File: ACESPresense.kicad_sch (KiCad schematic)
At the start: 16 parts, among them U1 ESP32-WROOM-32D

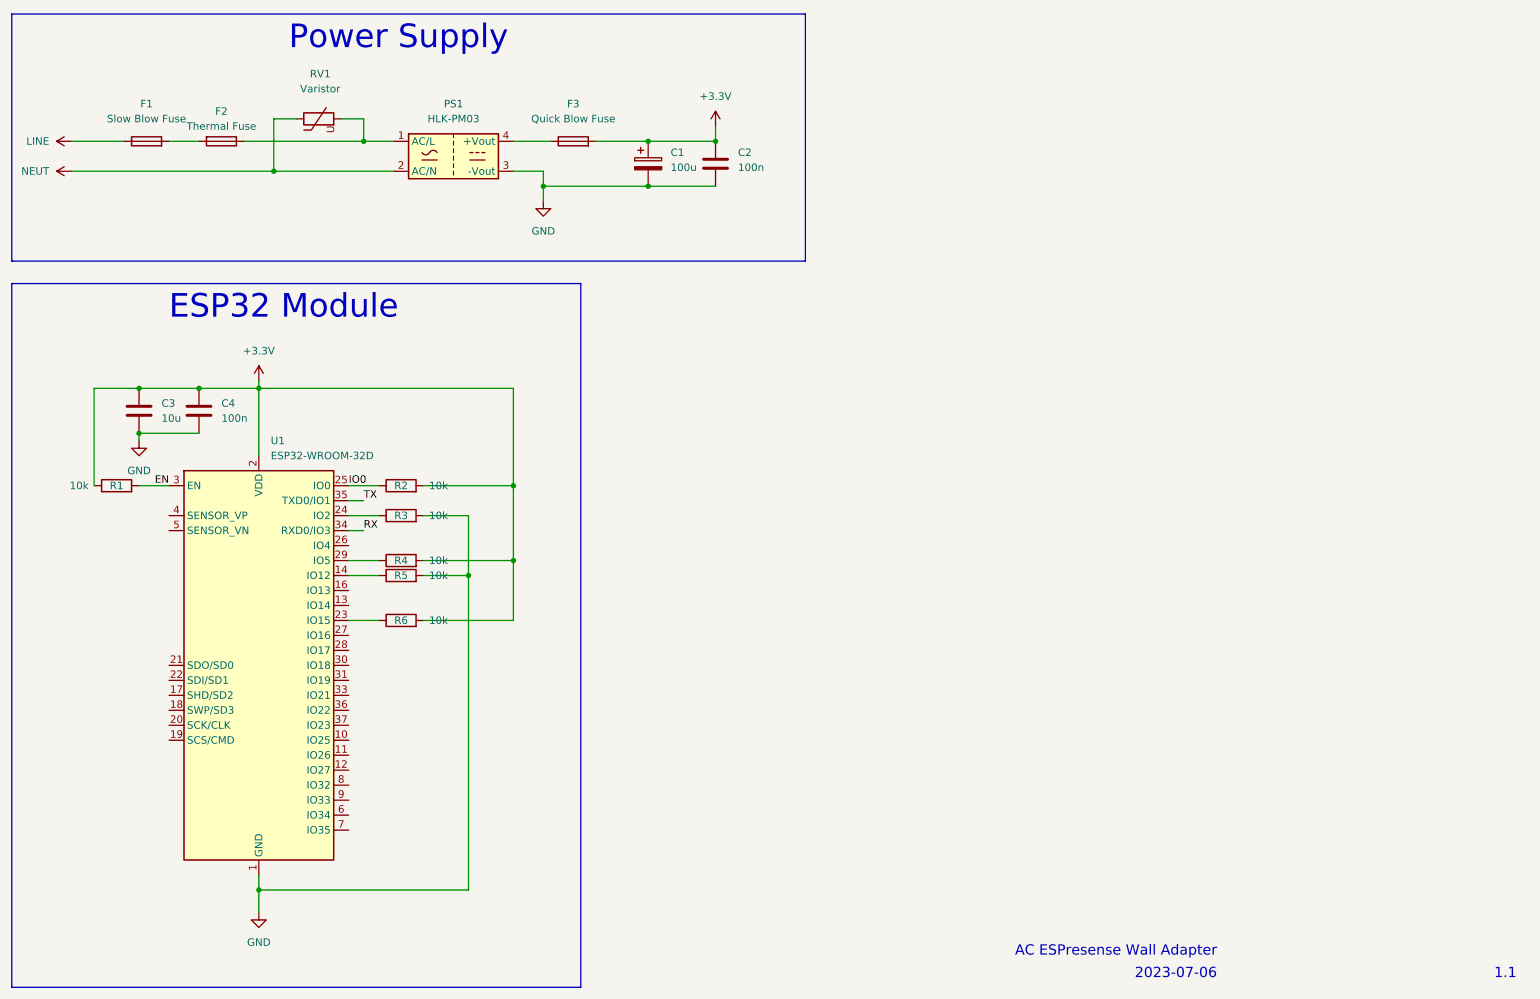
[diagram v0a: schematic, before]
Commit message: Added test points and fixed file names internally
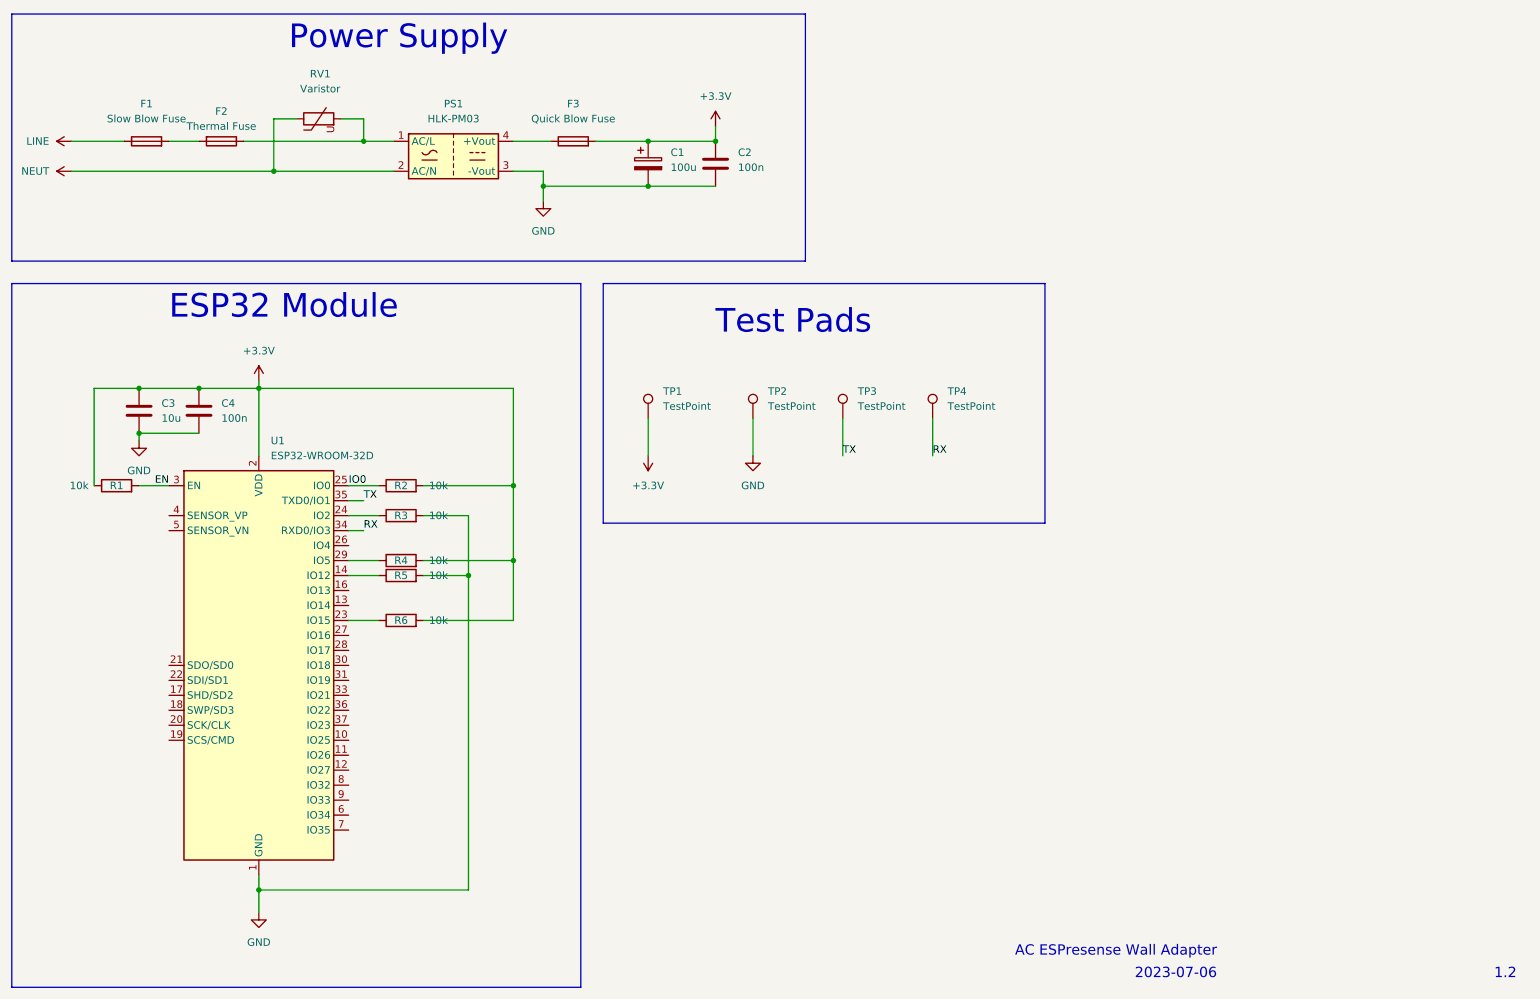
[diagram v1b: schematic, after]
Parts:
- added TP1, TP2, TP3, TP4: TestPoint, TestPoint:TestPoint_Pad_D2.0mm, symbol Connector:TestPoint
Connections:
- net +3.3V: now also TP1.1
- net GND: now also TP2.1
- net RX: now also TP4.1
- net TX: now also TP3.1
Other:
- note added: "1.2"
- note added: "Test Pads"
- note removed: "1.1"
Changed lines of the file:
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@@
+    (stroke (width 0) (type default))
+  )
+  (wire (pts (xy 124.46 99.06) (xy 124.46 105.41))
     (stroke (width 0) (type default))
   )
@@
     (stroke (width 0) (type default))
   )
+  (wire (pts (xy 142.24 99.06) (xy 142.24 105.41))
+    (stroke (width 0) (type default))
+  )
   (wire (pts (xy 106.68 59.69) (xy 124.46 59.69))
     (stroke (width 0) (type default))
@@
     (stroke (width 0) (type default))
   )
+  (wire (pts (xy 172.72 99.06) (xy 172.72 105.41))
+    (stroke (width 0) (type default))
+  )
   (wire (pts (xy 73.66 113.03) (xy 76.2 113.03))
     (stroke (width 0) (type default))
@@
     (stroke (width 0) (type default))
   )
+  (wire (pts (xy 157.48 99.06) (xy 157.48 105.41))
+    (stroke (width 0) (type default))
+  )
   (wire (pts (xy 135.89 49.53) (xy 135.89 52.07))
     (stroke (width 0) (type default))
@@
     (stroke (width 0) (type default))
     (fill (type none))
+  )
+  (rectangle (start 116.84 76.2) (end 191.77 116.84)
+    (stroke (width 0) (type default))
+    (fill (type none))
+  )
+  (text "Test Pads" (at 135.89 85.09 0)
+    (effects (font (size 4 4)) (justify left bottom))
   )
   (text "Power Supply" (at 63.5 36.83 0)
@@
     (effects (font (size 1.75 1.75)) (justify left bottom))
   )
-  (text "1.1" (at 267.97 194.31 0)
+  (text "1.2" (at 267.97 194.31 0)
     (effects (font (size 1.75 1.75)) (justify left bottom))
   )
@@
   )
   (label "RX" (at 76.2 118.11 0) (fields_autoplaced)
+    (effects (font (size 1.27 1.27)) (justify left bottom))
+  )
+  (label "TX" (at 157.48 105.41 0) (fields_autoplaced)
+    (effects (font (size 1.27 1.27)) (justify left bottom))
+  )
+  (label "RX" (at 172.72 105.41 0) (fields_autoplaced)
     (effects (font (size 1.27 1.27)) (justify left bottom))
   )
@@
     )
   )
+  (symbol (lib_id "Connector:TestPoint") (at 124.46 99.06 0) (unit 1)
+    (in_bom yes) (on_board yes) (dnp no) (fields_autoplaced)
+    (property "Reference" "TP1" (at 127 94.488 0)
+      (effects (font (size 1.27 1.27)) (justify left))
+    )
+    (property "Value" "TestPoint" (at 127 97.028 0)
+      (effects (font (size 1.27 1.27)) (justify left))
+    )
+    (property "Footprint" "TestPoint:TestPoint_Pad_D2.0mm" (at 129.54 99.06 0)
+      (effects (font (size 1.27 1.27)) hide)
+    )
+    (property "Datasheet" "~" (at 129.54 99.06 0)
+      (effects (font (size 1.27 1.27)) hide)
+    )
+    (pin "1")
+    (instances
+      (project "ACESPresense"
+        (path "/4af9e4e0-c69e-4ce2-89ff-dc3df65e601d"
+          (reference "TP1") (unit 1)
+        )
+      )
+    )
+  )
+  (symbol (lib_id "power:GND") (at 142.24 105.41 0) (unit 1)
+    (in_bom yes) (on_board yes) (dnp no) (fields_autoplaced)
+    (property "Reference" "#PWR02" (at 142.24 111.76 0)
+      (effects (font (size 1.27 1.27)) hide)
+    )
+    (property "Value" "GND" (at 142.24 110.49 0)
+      (effects (font (size 1.27 1.27)))
+    )
+    (property "Footprint" "" (at 142.24 105.41 0)
+      (effects (font (size 1.27 1.27)) hide)
+    )
+    (property "Datasheet" "" (at 142.24 105.41 0)
+      (effects (font (size 1.27 1.27)) hide)
+    )
+    (pin "1")
+    (instances
+      (project "ACESPresense"
+        (path "/4af9e4e0-c69e-4ce2-89ff-dc3df65e601d"
+          (reference "#PWR02") (unit 1)
+        )
+      )
+    )
+  )
   (symbol (lib_id "power:LINE") (at 26.67 52.07 90) (unit 1)
     (in_bom yes) (on_board yes) (dnp no) (fields_autoplaced)
@@
     )
   )
+  (symbol (lib_id "power:+3.3V") (at 124.46 105.41 180) (unit 1)
+    (in_bom yes) (on_board yes) (dnp no) (fields_autoplaced)
+    (property "Reference" "#PWR01" (at 124.46 101.6 0)
+      (effects (font (size 1.27 1.27)) hide)
+    )
+    (property "Value" "+3.3V" (at 124.46 110.49 0)
+      (effects (font (size 1.27 1.27)))
+    )
+    (property "Footprint" "" (at 124.46 105.41 0)
+      (effects (font (size 1.27 1.27)) hide)
+    )
+    (property "Datasheet" "" (at 124.46 105.41 0)
+      (effects (font (size 1.27 1.27)) hide)
+    )
+    (pin "1")
+    (instances
+      (project "ACESPresense"
+        (path "/4af9e4e0-c69e-4ce2-89ff-dc3df65e601d"
+          (reference "#PWR01") (unit 1)
+        )
+      )
+    )
+  )
   (symbol (lib_id "Device:Fuse") (at 39.37 52.07 90) (unit 1)
     (in_bom yes) (on_board yes) (dnp no) (fields_autoplaced)
@@
     )
   )
+  (symbol (lib_id "Connector:TestPoint") (at 172.72 99.06 0) (unit 1)
+    (in_bom yes) (on_board yes) (dnp no) (fields_autoplaced)
+    (property "Reference" "TP4" (at 175.26 94.488 0)
+      (effects (font (size 1.27 1.27)) (justify left))
+    )
+    (property "Value" "TestPoint" (at 175.26 97.028 0)
+      (effects (font (size 1.27 1.27)) (justify left))
+    )
+    (property "Footprint" "TestPoint:TestPoint_Pad_D2.0mm" (at 177.8 99.06 0)
+      (effects (font (size 1.27 1.27)) hide)
+    )
+    (property "Datasheet" "~" (at 177.8 99.06 0)
+      (effects (font (size 1.27 1.27)) hide)
+    )
+    (pin "1")
+    (instances
+      (project "ACESPresense"
+        (path "/4af9e4e0-c69e-4ce2-89ff-dc3df65e601d"
+          (reference "TP4") (unit 1)
+        )
+      )
+    )
+  )
   (symbol (lib_id "Device:C_Polarized") (at 124.46 55.88 0) (unit 1)
     (in_bom yes) (on_board yes) (dnp no) (fields_autoplaced)
@@
     )
   )
+  (symbol (lib_id "Connector:TestPoint") (at 157.48 99.06 0) (unit 1)
+    (in_bom yes) (on_board yes) (dnp no)
+    (property "Reference" "TP3" (at 160.02 94.488 0)
+      (effects (font (size 1.27 1.27)) (justify left))
+    )
+    (property "Value" "TestPoint" (at 160.02 97.028 0)
+      (effects (font (size 1.27 1.27)) (justify left))
+    )
+    (property "Footprint" "TestPoint:TestPoint_Pad_D2.0mm" (at 162.56 99.06 0)
+      (effects (font (size 1.27 1.27)) hide)
+    )
+    (property "Datasheet" "~" (at 162.56 99.06 0)
+      (effects (font (size 1.27 1.27)) hide)
+    )
+    (pin "1")
+    (instances
+      (project "ACESPresense"
+        (path "/4af9e4e0-c69e-4ce2-89ff-dc3df65e601d"
+          (reference "TP3") (unit 1)
+        )
+      )
+    )
+  )
   (symbol (lib_id "Converter_ACDC:HLK-PM03") (at 91.44 54.61 0) (unit 1)
     (in_bom yes) (on_board yes) (dnp no) (fields_autoplaced)
@@
         )
       )
+    )
+  )
+  (symbol (lib_id "Connector:TestPoint") (at 142.24 99.06 0) (unit 1)
+    (in_bom yes) (on_board yes) (dnp no) (fields_autoplaced)
+    (property "Reference" "TP2" (at 144.78 94.488 0)
+      (effects (font (size 1.27 1.27)) (justify left))
+    )
+    (property "Value" "TestPoint" (at 144.78 97.028 0)
+      (effects (font (size 1.27 1.27)) (justify left))
+    )
+    (property "Footprint" "TestPoint:TestPoint_Pad_D2.0mm" (at 147.32 99.06 0)
+      (effects (font (size 1.27 1.27)) hide)
+    )
+    (property "Datasheet" "~" (at 147.32 99.06 0)
+      (effects (font (size 1.27 1.27)) hide)
+    )
+    (pin "1")
+    (instances
+      (project "ACESPresense"
+        (path "/4af9e4e0-c69e-4ce2-89ff-dc3df65e601d"
+          (reference "TP2") (unit 1)
+        )
+      )
